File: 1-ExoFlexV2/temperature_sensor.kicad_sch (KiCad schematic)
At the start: 18 parts, among them U68 SN74LVC1G32DBVR

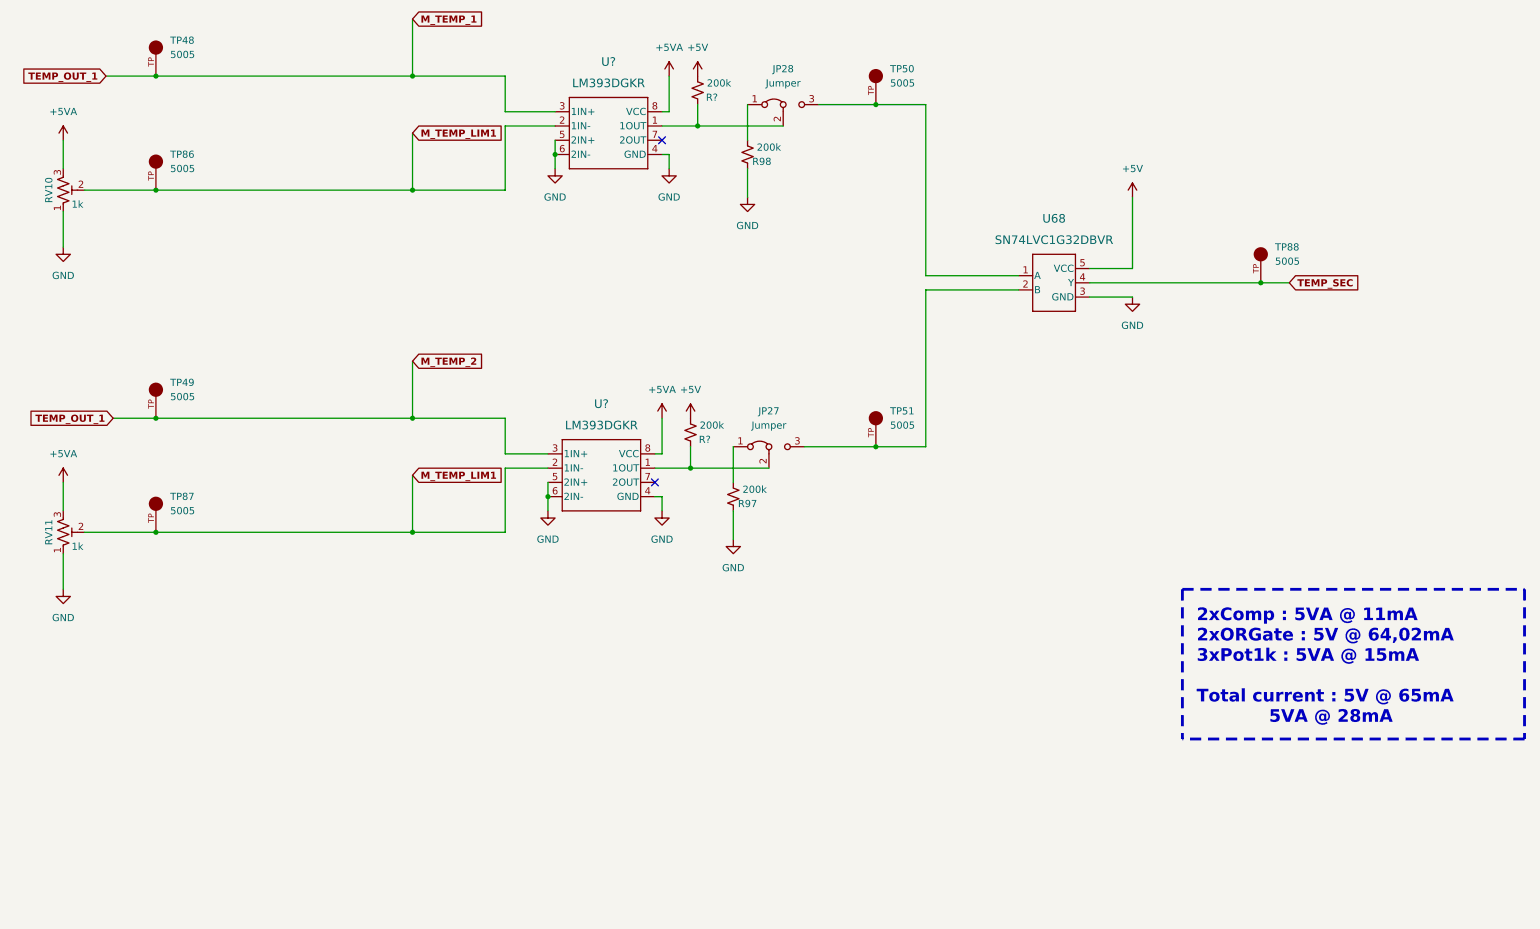
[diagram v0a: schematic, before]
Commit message: Chokes et RC
- Ajout des RF chokes
- Changement des résistance pour 0805
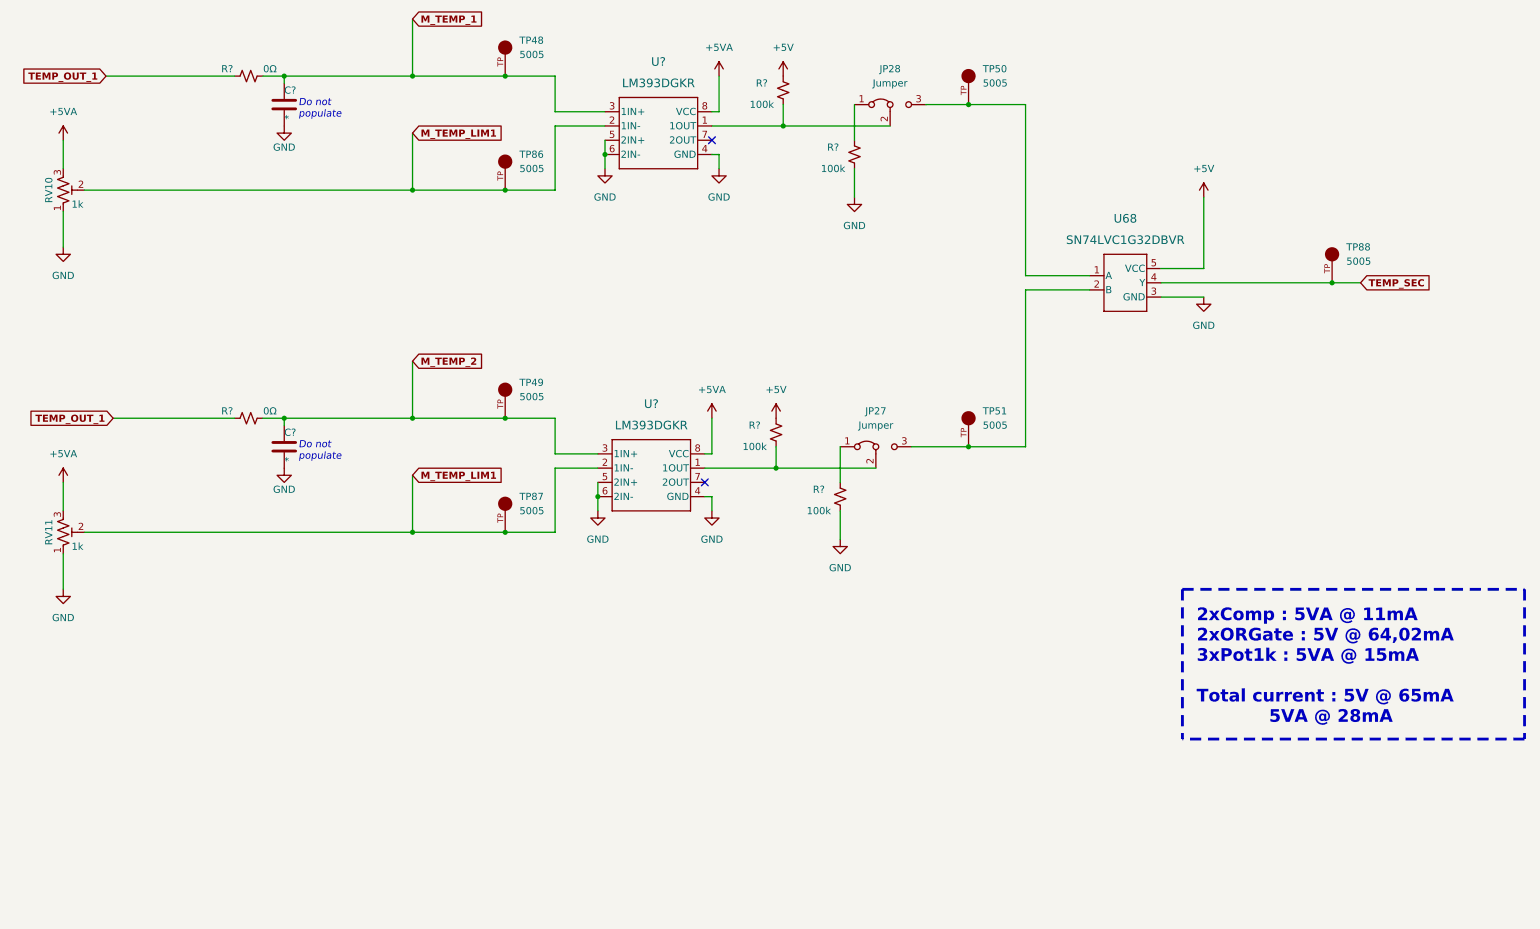
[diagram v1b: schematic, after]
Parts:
- removed R97, R98, R? (x2): 200k, Resistor_SMD:R_0603_1608Metric, symbol Device:R_Small_US
- added C? (x2): *, Capacitor_SMD:C_0805_2012Metric, symbol Device:C
- added R? (x4): 100k, Resistor_SMD:R_0805_2012Metric, symbol Device:R_Small_US
- added R? (x2): 0Ω, Resistor_SMD:R_0805_2012Metric, symbol Device:R_Small_US
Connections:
- net +5V: now also R?.1, R?.1
- net GND: now also C?.2, C?.2, R?.2, R?.2
- net M_TEMP_1: now also C?.1, R?.2; no longer TP49.TP, U?.3 (1IN+)
- net at JP28.1 (A): now also R?.1
- net at JP28.2 (C), U?.1 (1OUT): now also R?.2
- net at JP27.2 (C), U?.1 (1OUT): now also R?.2
- net at JP27.1 (A): now also R?.1
- new net M_TEMP_2: C?.1, R?.2, TP49.TP, U?.3 (1IN+)
- new net TEMP_OUT_1: R?.1, R?.1
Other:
- note added: "Do not populate"
- moved on the sheet: JP27, JP28, TP48, TP49, TP50, TP51, TP86, TP87, TP88, U68, U?

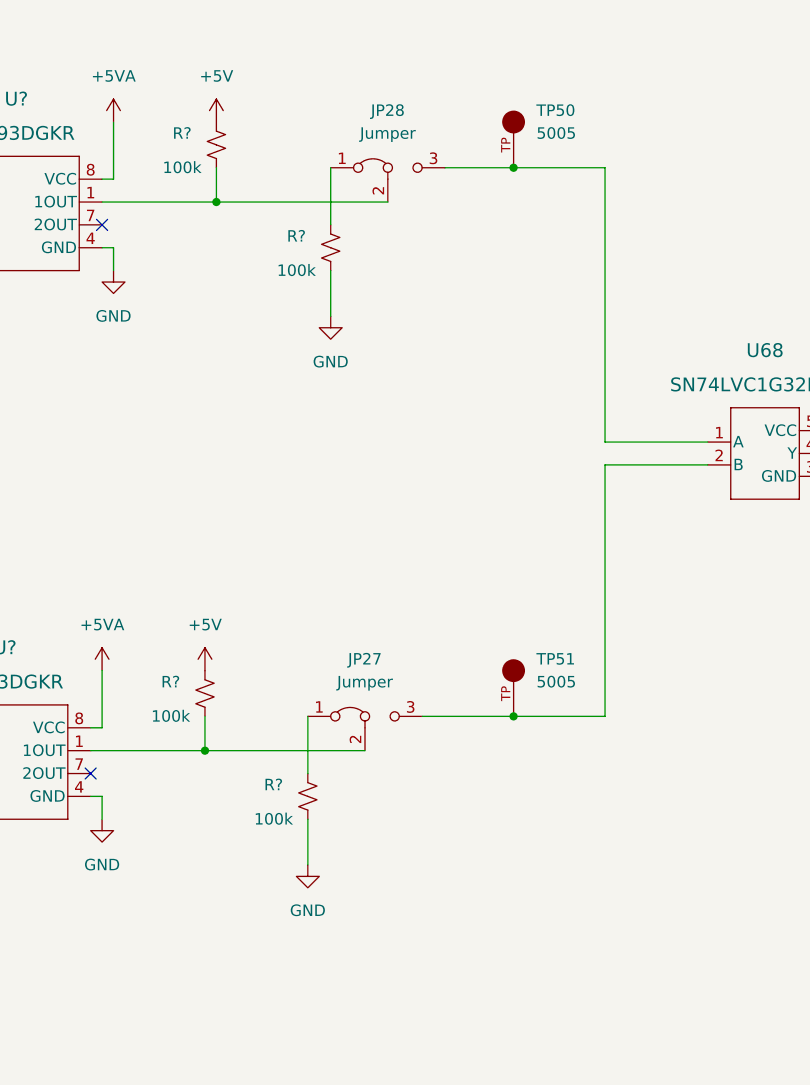
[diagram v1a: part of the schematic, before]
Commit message: Trimmer et jumper
-Changement de symbole de jumper
-Ajout des des trimmer aux endroits nécessaires
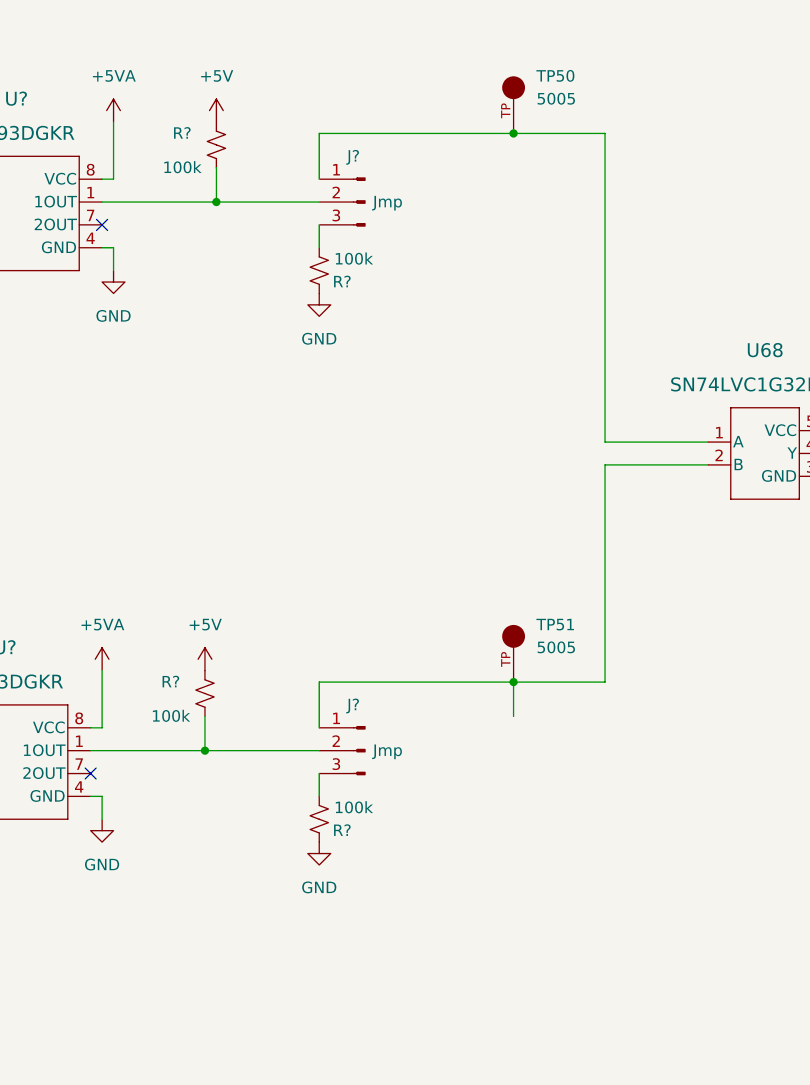
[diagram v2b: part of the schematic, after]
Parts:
- removed JP27, JP28: Jumper, Connector_PinHeader_2.54mm:PinHeader_1x03_P2.54mm_Vertical, symbol Jumper:Jumper_3_Bridged12
- removed R? (x2): 100k, Resistor_SMD:R_0805_2012Metric, symbol Device:R_Small_US
- added J? (x2): Jmp, symbol Connector:Conn_01x03_Male
- added R? (x2): 100k, Resistor_SMD:R_0805_2012Metric, symbol Device:R_Small_US
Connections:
- net GND: now also R?.2, R?.2
- net at R?.2, U?.1 (1OUT): now also J?.2 (Pin_2) (x2)
- net at TP51.TP, U68.2 (B): now also J?.1 (Pin_1)
- net at TP50.TP, U68.1 (A): now also J?.1 (Pin_1)
- new net: J?.3 (Pin_3), R?.1 (x2)
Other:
- moved on the sheet: TP50, TP51

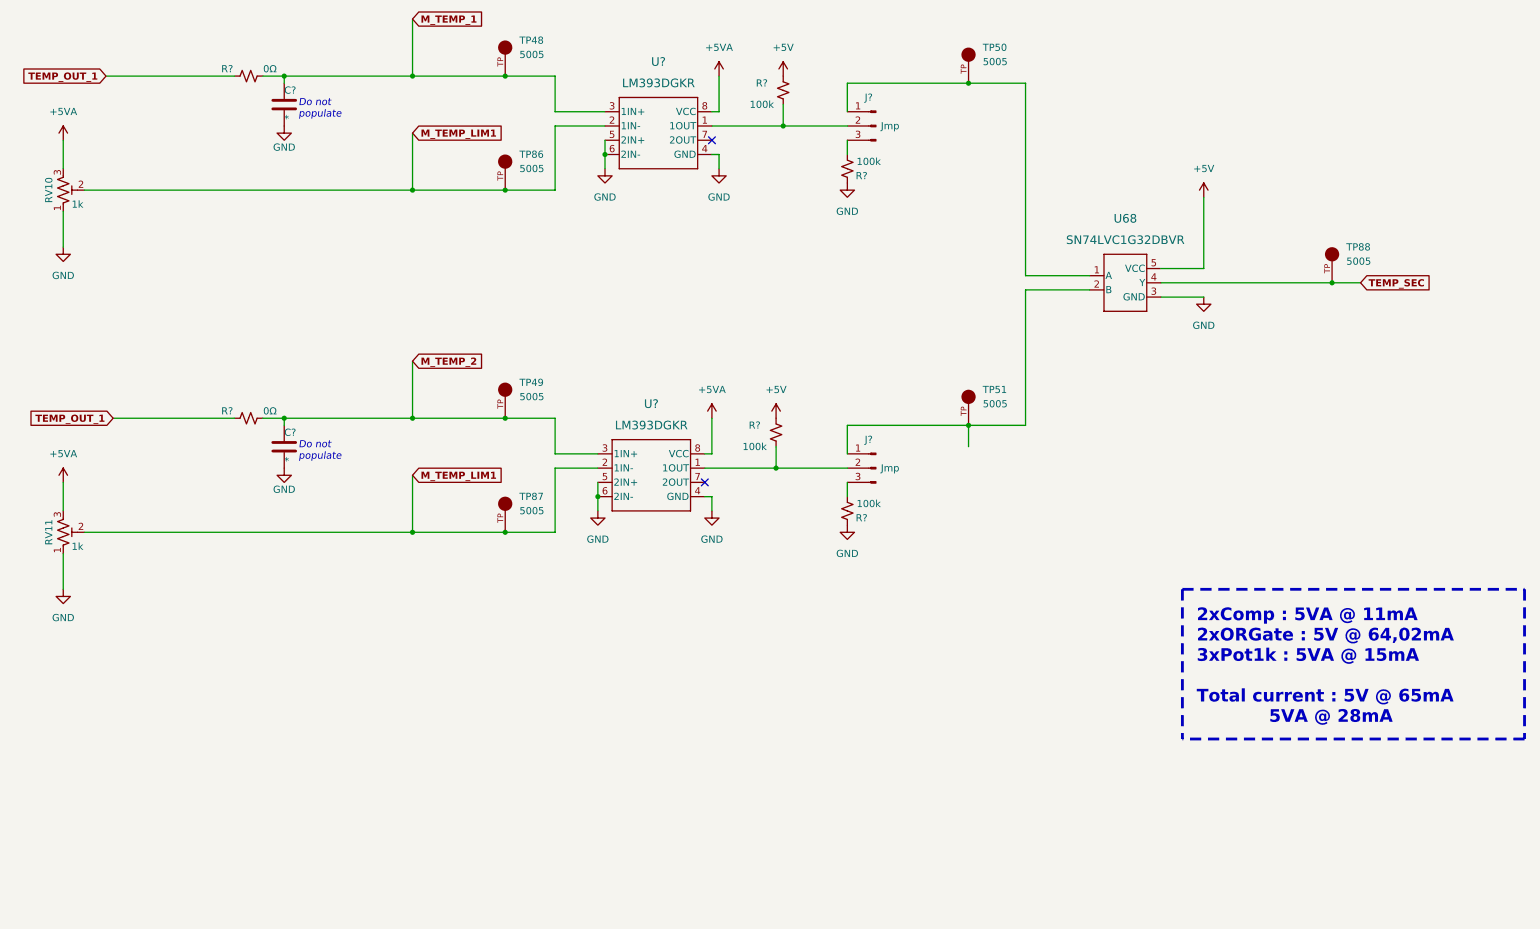
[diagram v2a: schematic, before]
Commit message: Test points et notes
- Ajout de tous les tests point nécessaires
-  Ajoute des sections de notes dans chaque page
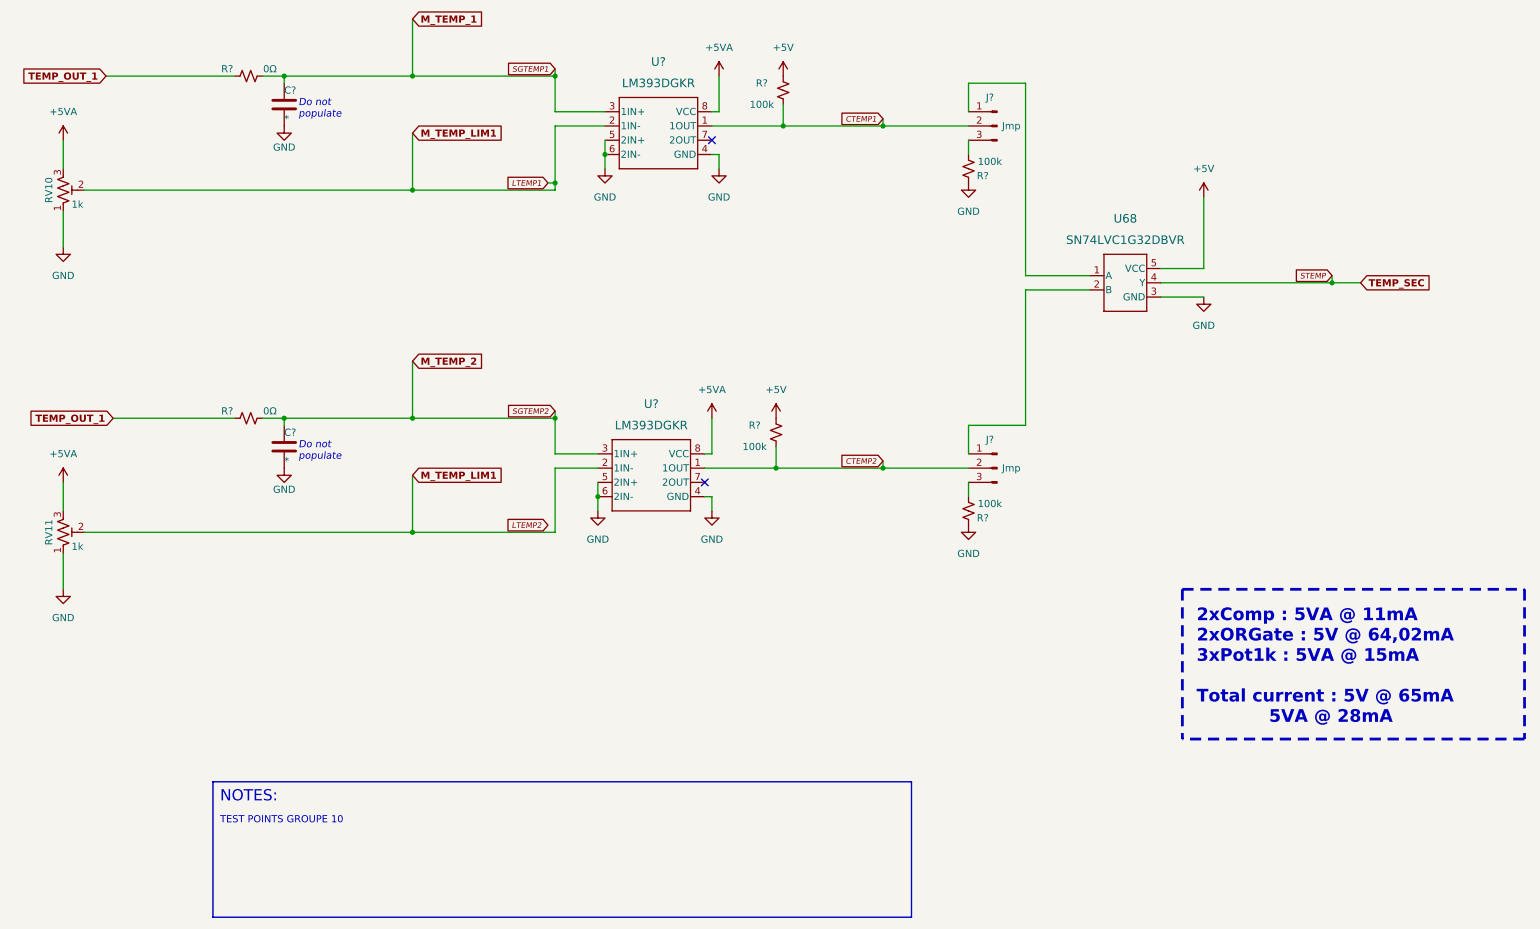
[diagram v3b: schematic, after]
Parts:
- removed TP48, TP49, TP50, TP51, TP86, TP87, TP88: 5005, FootPrint:KEYSTONE_5005, symbol SymLib:5005
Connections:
- net CTEMP2: now reaches J?.2 (Pin_2), R?.2, U?.1 (1OUT)
- net CTEMP1: now reaches J?.2 (Pin_2), R?.2, U?.1 (1OUT)
- net M_TEMP_LIM1 renamed LTEMP1
- net TEMP_SEC renamed STEMP
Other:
- note added: "NOTES:"
- note added: "TEST POINTS GROUPE 10"
- moved on the sheet: J?, R?

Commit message: Schématisation terminée
- Schéma terminé
- Passage vers le PCB
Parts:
- C52, C53: renamed from C?; value * -> 10nF 10V X5R; footprint Capacitor_SMD:C_0805_2012Metric -> Capacitor_SMD:C_01005_0402Metric; DESCRIPTION (none) -> 10000 pF ±10% 10V Ceramic Capacitor X5R 01005 (0402 Metric); MANUFACTURER (none) -> Murata Electronics; NOTES (none) -> DO NOT POPULATE; PACKAGE (none) -> 01005 (0402 Metric); PART NUMBER (none) -> GRM022R61A103KE19L; TYPE (none) -> SMD
- J109, J110: renamed from J?; value Jmp -> Jumper; footprint (none) -> Connector_PinSocket_2.54mm:PinSocket_1x03_P2.54mm_Vertical; DESCRIPTION (none) -> CONN HEADER VERT 3POS 2.54MM; MANUFACTURER (none) -> Würth Elektronik; PACKAGE (none) -> Square 0.100" (2.54mm); PART NUMBER (none) -> 61300311121; TYPE (none) -> Through Hole
- R164, R165: renamed from R?; DESCRIPTION (none) -> 0 Ohms Jumper Chip Resistor 0805 (2012 Metric) Automotive A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; MANUFACTURER (none) -> Panasonic Electronic Components; PACKAGE (none) -> 0805 (2012 Metric); PART NUMBER (none) -> ERJ-6GEY0R00V; TYPE (none) -> SMD
- R166, R167, R168, R169: renamed from R?; value 100k -> 100k 5% 1/8W; DESCRIPTION (none) -> 100 kOhms ±5% 0.125W, 1/8W Chip Resistor 0805 (2012 Metric)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; MANUFACTURER (none) -> Panasonic Electronic Components; PACKAGE (none) -> 0805 (2012 Metric); PART NUMBER (none) -> ERJ-6GEYJ104V; TYPE (none) -> SMD
- RV33: renamed from RV10; value 1k -> Trim 1k; DESCRIPTION (none) -> Trimmer 1k 0,5W PC PIN TOP; MANUFACTURER (none) -> Bourns Inc.; PACKAGE (none) -> Rectangular - 0.275" x 0.260" Face; PART NUMBER (none) -> 3362P-1-102LF; TYPE (none) -> Through Hole
- RV34: renamed from RV11; value 1k -> Trim 1k; DESCRIPTION (none) -> Trimmer 1k 0,5W PC PIN TOP; MANUFACTURER (none) -> Bourns Inc.; PACKAGE (none) -> Rectangular - 0.275" x 0.260" Face; PART NUMBER (none) -> 3362P-1-102LF; TYPE (none) -> Through Hole
- U85, U86: renamed from U?; value LM393DGKR -> COMP; footprint DGK8 -> FootPrint:DGK8; DESCRIPTION (none) -> Comparator General Purpose Open-Collector, Rail-to-Rail 8-V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; MANUFACTURER (none) -> Texas Instruments; PACKAGE (none) -> 8-TSSOP, 8-MSOP (0.118", 3.00mm Width); PART NUMBER (none) -> LM393DGKR; TYPE (none) -> SMD
- U87: renamed from U68; value SN74LVC1G32DBVR -> OR Gate; DESCRIPTION (none) -> OR Gate IC 1 Channel SOT-23-5; MANUFACTURER (none) -> Texas Instruments; PACKAGE (none) -> SC-74A, SOT-753; PART NUMBER (none) -> SN74LVC1G32DBVR; TYPE (none) -> SMD
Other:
- note added: "2xComp : 5VA @ 51,6mA 2xORGate : 5V @ 64,02mA 2xPot1k : 5VA @ 200mA 4x100k : 5V @ 0,2mA Total current : 5V @ 69mA 5VA @ 256mA"
- note removed: "2xComp : 5VA @ 11mA 2xORGate : 5V @ 64,02mA 3xPot1k : 5VA @ 15mA Total current : 5V @ 65mA 5VA @ 28mA"
- moved on the sheet: J109, R168
